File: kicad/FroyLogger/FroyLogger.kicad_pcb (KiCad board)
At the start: 2 copper layers, 78.9 x 47.2 mm, 33 parts, among them J1 Conn_01x08, J2 Conn_01x04, J3 Conn_01x06, Q1 Q_NPN_BEC, Q2 Q_NPN_BEC, Q3 Q_NPN_BEC, SW1 SW_MEC_5E, U1 ESP-WROOM-02U__4MB_, U2 BME280, U3 MCP7940N-xSN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

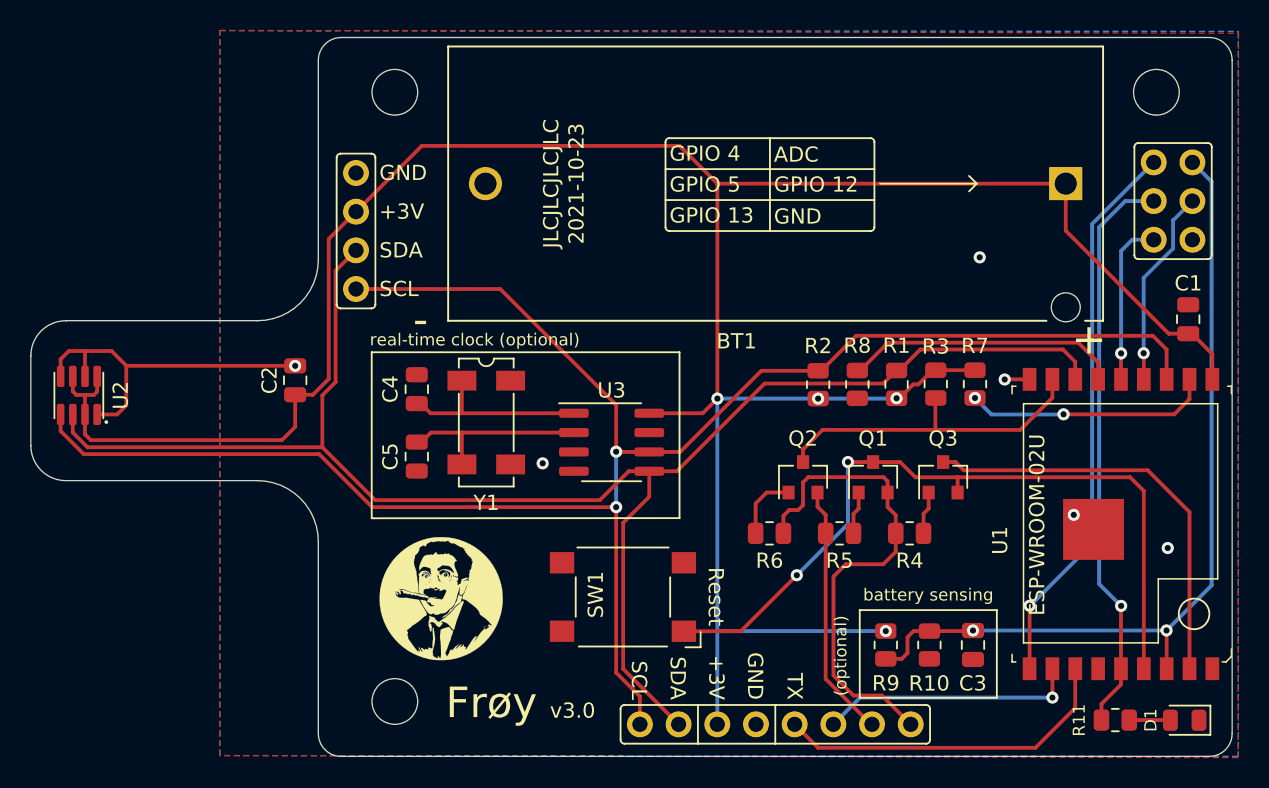
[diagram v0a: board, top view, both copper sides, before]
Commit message: FroyLogger 3.0.1, better crystal footprint
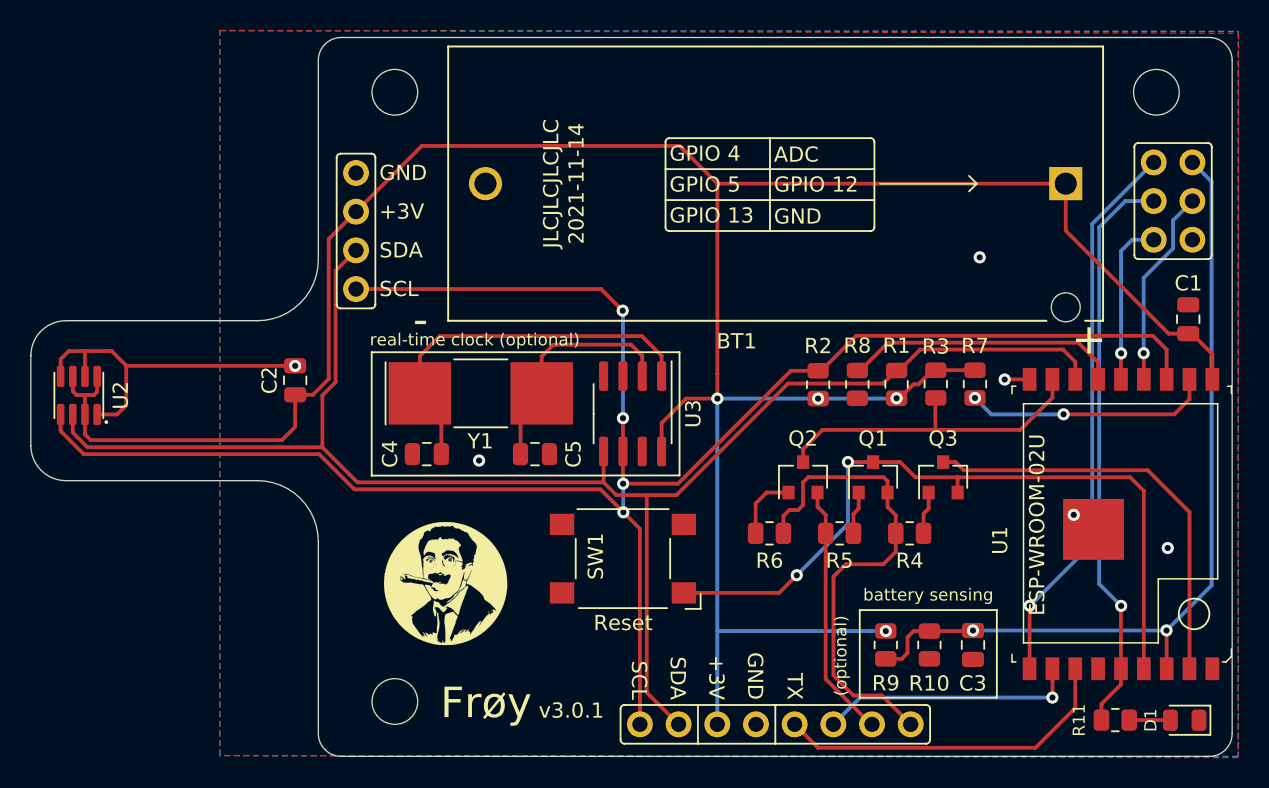
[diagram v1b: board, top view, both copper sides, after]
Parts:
- Y1: footprint Crystal:Crystal_SMD_SeikoEpson_MC306-4Pin_8.0x3.2mm -> Crystal:Crystal_SMD_SeikoEpson_MC405-2Pin_9.6x4.1mm
- moved C5 7.76 mm to (156.8, 62.4), turned to 0 degrees
- moved C4 4.32 mm to (149.7, 62.4), turned to 180 degrees
- moved SW1 2.52 mm to (162.6, 69.2)
- moved U3 2.32 mm to (163.2, 59.7), turned to 270 degrees
- moved Y1 1.95 mm to (153.2, 58.4), turned to 0 degrees
- moved G1 1.03 mm to (150.9, 70.8)
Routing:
- net Net-(C4-Pad1): track 12.7 -> 25.3 mm
- net /I2C_CLK: track 123.3 -> 128.2 mm, vias 2 -> 4
- net Net-(C5-Pad1): track 12.7 -> 15.5 mm
- net +3V3: track 173.2 -> 174.5 mm
- net /I2C_SDA: track 107.5 -> 106.3 mm
- net /RST: track 50.7 -> 49.6 mm
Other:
- board text added: "2021-11-14"
- board text added: "ESP-WROOM-02U/D BME280/680, BMP180 MCP7940N-xSN Omron B3FS-10xx Keystone 1051 MC-405 32.768 kHz"
- board text added: "v3.0.1"
- board text removed: "2021-10-23"
- board text removed: "ESP-WROOM-02U/D BME280/680, BMP180 MCP7940N-xSN Omron B3FS-10xx Keystone 1051 MC-306 32.768 kHz"
- board text removed: "v3.0"
